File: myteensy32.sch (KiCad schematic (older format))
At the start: 1 part

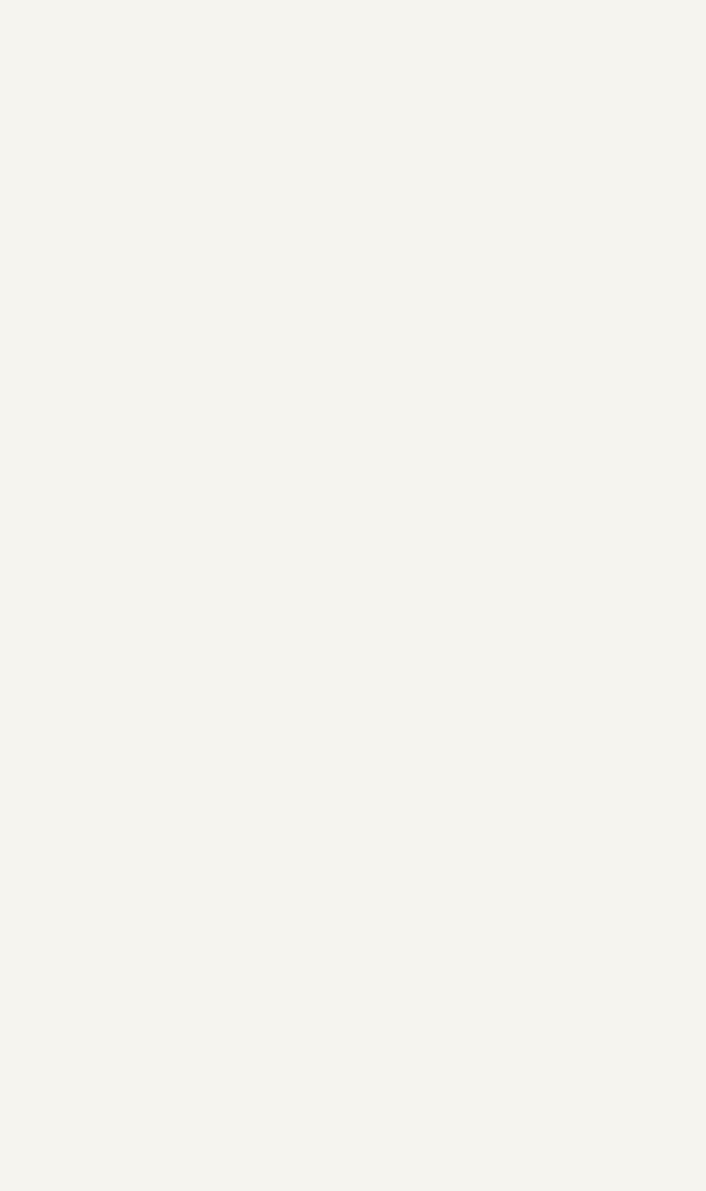
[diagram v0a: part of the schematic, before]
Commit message: add sym mk20dx256vlh7
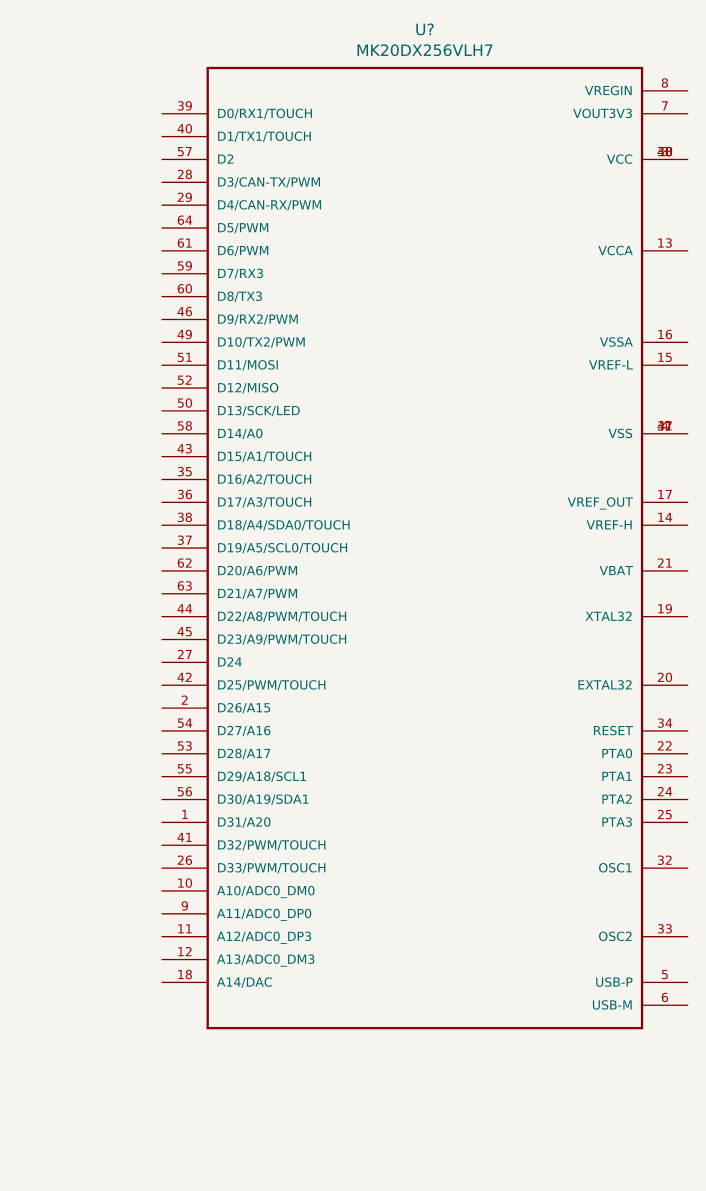
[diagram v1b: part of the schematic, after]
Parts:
- added U?: MK20DX256VLH7, QFP50P1200X1200X160-64N, symbol mylib:MK20DX256VLH7
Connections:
- new net: U?.3 (VCC), U?.30 (VCC), U?.48 (VCC)
- new net: U?.31 (VSS), U?.4 (VSS), U?.47 (VSS)
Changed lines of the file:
@@
+	1    0    0    -1
+$EndComp
+$Comp
+L mylib:MK20DX256VLH7 U?
+U 1 1 5F4A22C6
+P 8050 3500
+F 0 "U?" H 8100 5867 50  0000 C CNN
+F 1 "MK20DX256VLH7" H 8100 5776 50  0000 C CNN
+F 2 "QFP50P1200X1200X160-64N" H 8050 3500 50  0001 L BNN
+F 3 "" H 8050 3500 50  0001 C CNN
+	1    8050 3500
 	1    0    0    -1
 $EndComp

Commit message: シンボルのの作り方が雑だったので心配したけど大丈夫そうだった。
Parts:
- removed U?: MK20DX256VLH7, QFP50P1200X1200X160-64N, symbol mylib:MK20DX256VLH7
- added U2: MK20DX256VLH7, mylib:QFP50P1200X1200X160-64N, symbol mylib:MK20DX256VLH7
- gave numbers to parts that had none: 1
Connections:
- net at U1.25 (PTB5/IRQ_16): now also U2.31 (VSS), U2.4 (VSS), U2.47 (VSS)
- new net: U2.3 (VCC), U2.30 (VCC), U2.48 (VCC)
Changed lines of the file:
@@
 $EndDescr
 $Comp
-L MCU_NXP_Kinetis:MKL04Z32VLC4 U?
+L MCU_NXP_Kinetis:MKL04Z32VLC4 U1
 U 1 1 5F49FA87
 P 4450 4650
-F 0 "U?" H 4450 6631 50  0000 C CNN
+F 0 "U1" H 4450 6631 50  0000 C CNN
 F 1 "MKL04Z32VLC4" H 4450 6540 50  0000 C CNN
 F 2 "Package_QFP:LQFP-32_7x7mm_P0.8mm" H 4600 3025 50  0001 L TNN
@@
 $EndComp
 $Comp
-L mylib:MK20DX256VLH7 U?
-U 1 1 5F4A22C6
-P 8050 3500
-F 0 "U?" H 8100 5867 50  0000 C CNN
-F 1 "MK20DX256VLH7" H 8100 5776 50  0000 C CNN
-F 2 "QFP50P1200X1200X160-64N" H 8050 3500 50  0001 L BNN
-F 3 "" H 8050 3500 50  0001 C CNN
-	1    8050 3500
+L mylib:MK20DX256VLH7 U2
+U 1 1 5F4A610C
+P 8250 4000
+F 0 "U2" H 8300 6367 50  0000 C CNN
+F 1 "MK20DX256VLH7" H 8300 6276 50  0000 C CNN
+F 2 "mylib:QFP50P1200X1200X160-64N" H 8250 4000 50  0001 L BNN
+F 3 "" H 8250 4000 50  0001 C CNN
+	1    8250 4000
 	1    0    0    -1
 $EndComp
+Wire Wire Line
+	9450 3400 10300 3400
+Wire Wire Line
+	10300 3400 10300 1400
+Wire Wire Line
+	10300 1400 6400 1400
+Wire Wire Line
+	6400 4150 5850 4150
+Wire Wire Line
+	6400 1400 6400 4150
 $EndSCHEMATC

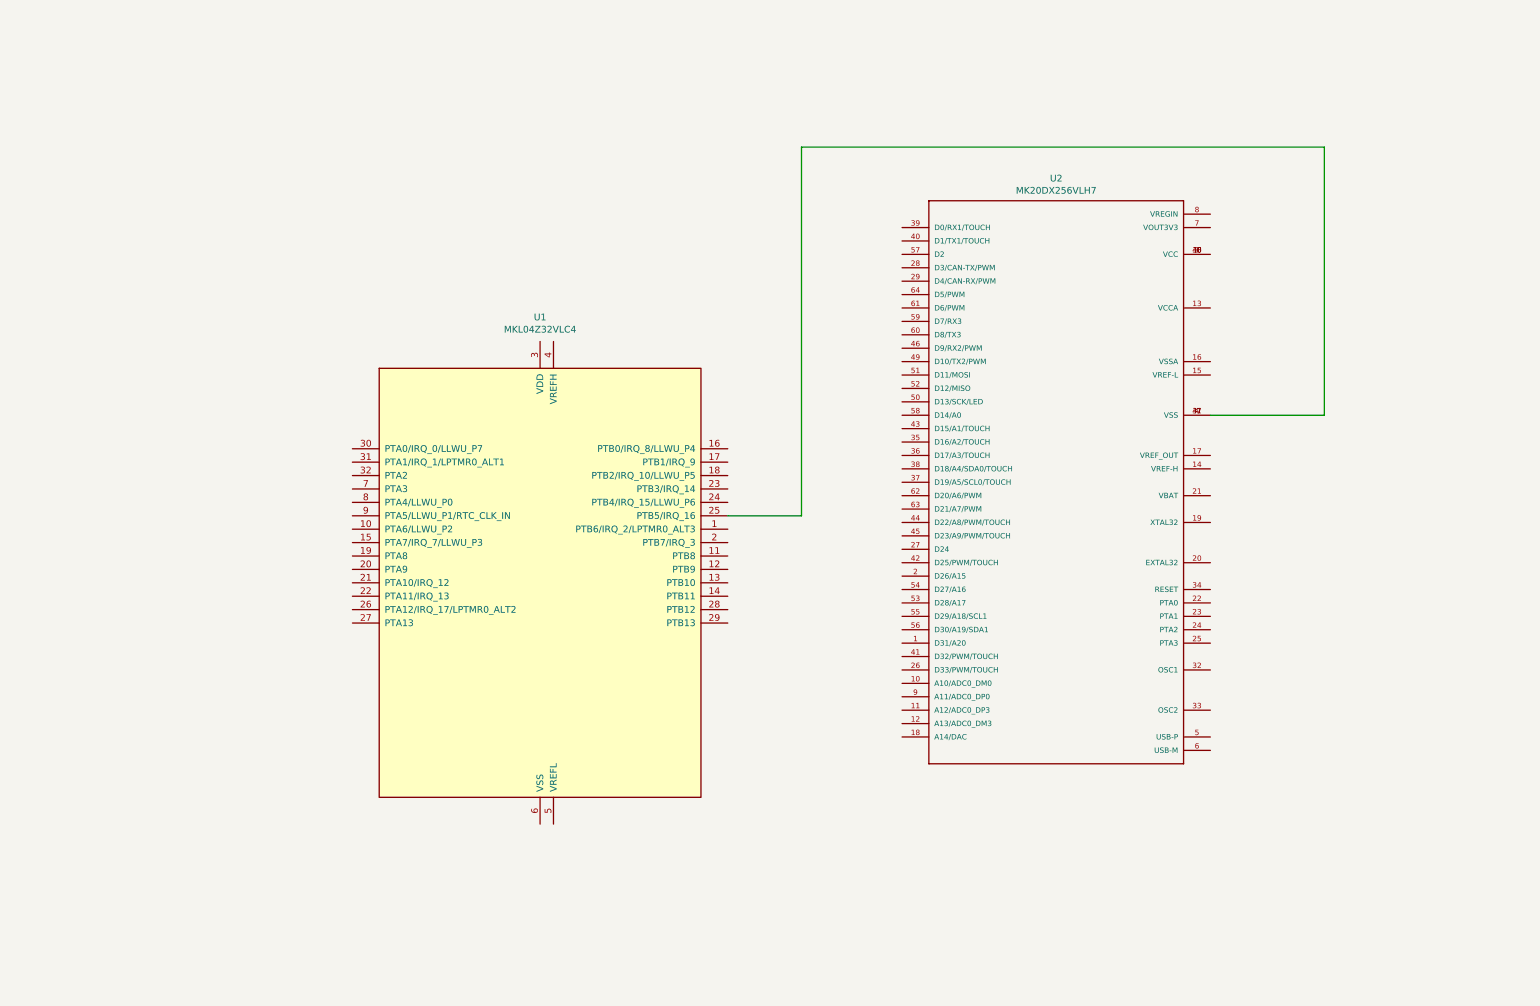
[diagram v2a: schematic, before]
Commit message: mkl04z32vlc4周辺の配線ができた
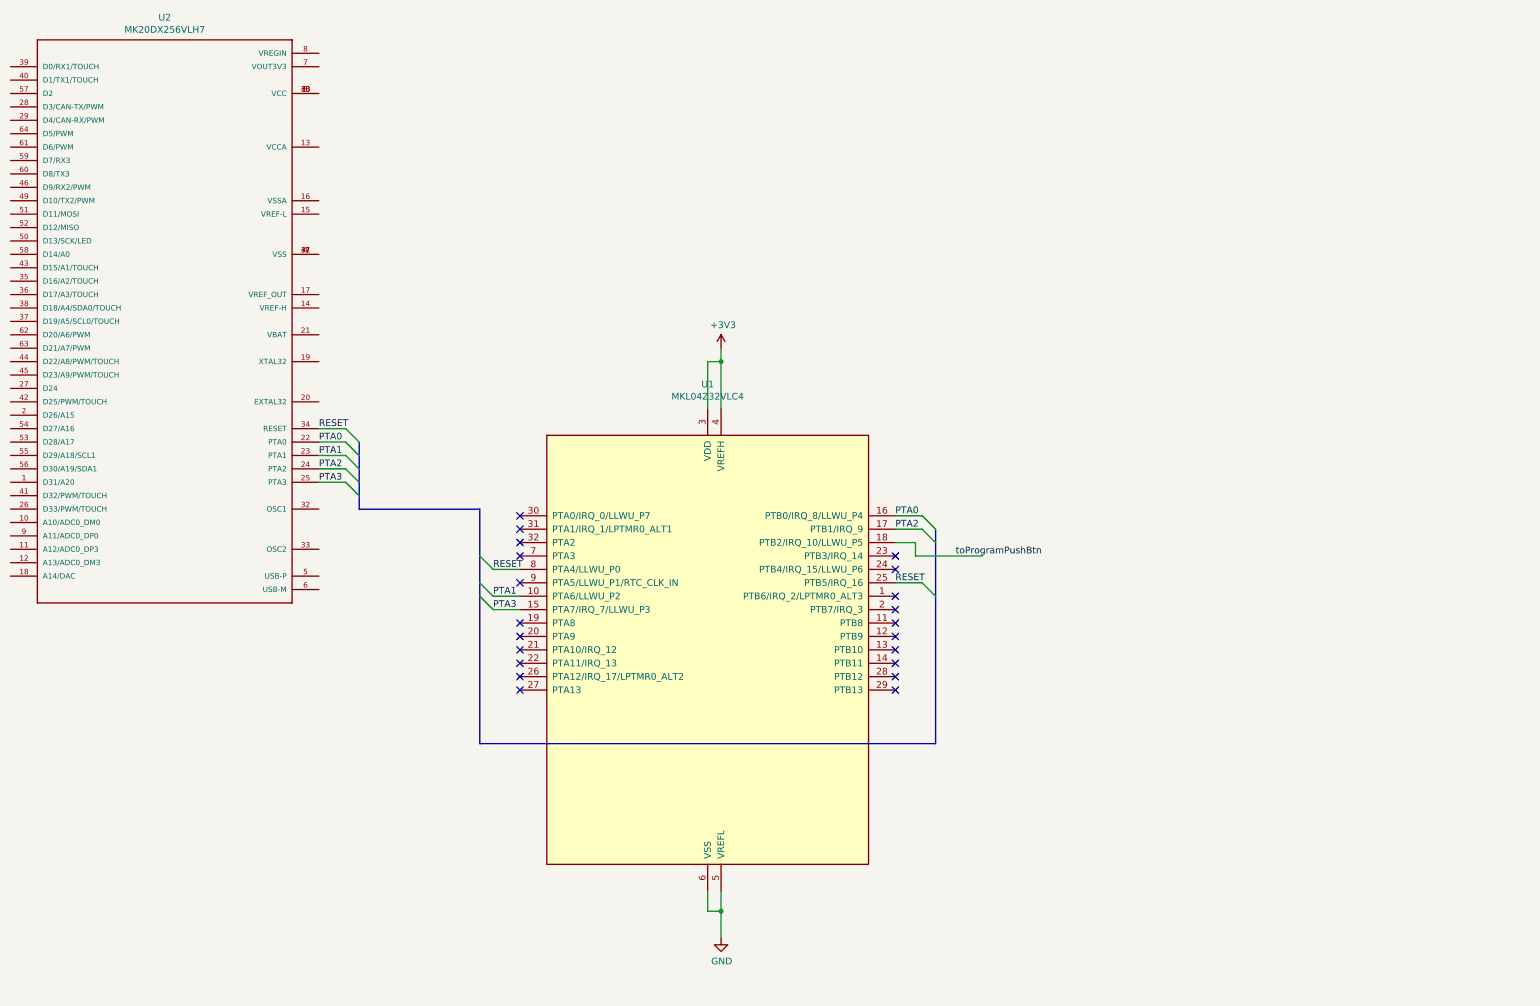
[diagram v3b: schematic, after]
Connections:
- net labels added: +3V3, GND, PTA0, PTA1, PTA2, PTA3, RESET, toProgramPushBtn
- wire segments 5 -> 22
- no-connect marks 0 -> 21
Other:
- moved on the sheet: U1, U2
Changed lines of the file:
@@
 $EndDescr
+$Comp
+L mylib:MK20DX256VLH7 U2
+U 1 1 5F4A610C
+P 1600 2800
+F 0 "U2" H 1650 5167 50  0000 C CNN
+F 1 "MK20DX256VLH7" H 1650 5076 50  0000 C CNN
+F 2 "mylib:QFP50P1200X1200X160-64N" H 1600 2800 50  0001 L BNN
+F 3 "" H 1600 2800 50  0001 C CNN
+	1    1600 2800
+	1    0    0    -1
+$EndComp
+Wire Wire Line
+	2800 3500 3000 3500
+Text Label 2800 3500 0    50   ~ 0
+RESET
+Wire Wire Line
+	2800 3600 3000 3600
+Wire Wire Line
+	2800 3700 3000 3700
+Wire Wire Line
+	2800 3800 3000 3800
+Wire Wire Line
+	2800 3900 3000 3900
+Text Label 2800 3600 0    50   ~ 0
+PTA0
+Text Label 2800 3700 0    50   ~ 0
+PTA1
+Text Label 2800 3800 0    50   ~ 0
+PTA2
+Text Label 2800 3900 0    50   ~ 0
+PTA3
+Entry Wire Line
+	3000 3500 3100 3600
+Entry Wire Line
+	3000 3600 3100 3700
+Entry Wire Line
+	3000 3700 3100 3800
+Entry Wire Line
+	3000 3800 3100 3900
+Entry Wire Line
+	3000 3900 3100 4000
+Wire Bus Line
+	3100 3600 3100 4100
+$Comp
+L power:GND #PWR?
+U 1 1 5F4B89CA
+P 5800 7300
+F 0 "#PWR?" H 5800 7050 50  0001 C CNN
+F 1 "GND" H 5805 7127 50  0000 C CNN
+F 2 "" H 5800 7300 50  0001 C CNN
+F 3 "" H 5800 7300 50  0001 C CNN
+	1    5800 7300
+	1    0    0    -1
+$EndComp
+Connection ~ 5800 7100
+Wire Bus Line
+	4000 4100 4000 5850
+Wire Bus Line
+	7400 4250 7400 5850
+Wire Wire Line
+	5800 7100 5800 7300
+Wire Wire Line
+	5800 7100 5800 6950
+Wire Wire Line
+	5700 7100 5800 7100
+Wire Wire Line
+	5700 6950 5700 7100
+Connection ~ 5800 3000
+Wire Wire Line
+	5800 2900 5800 3000
+$Comp
+L power:+3V3 #PWR?
+U 1 1 5F4B7C1C
+P 5800 2900
+F 0 "#PWR?" H 5800 2750 50  0001 C CNN
+F 1 "+3V3" H 5815 3073 50  0000 C CNN
+F 2 "" H 5800 2900 50  0001 C CNN
+F 3 "" H 5800 2900 50  0001 C CNN
+	1    5800 2900
+	1    0    0    -1
+$EndComp
+Wire Wire Line
+	5800 3000 5800 3350
+Wire Wire Line
+	5700 3000 5800 3000
+Wire Wire Line
+	5700 3350 5700 3000
+NoConn ~ 4300 4950
+NoConn ~ 4300 5050
+NoConn ~ 4300 5150
+NoConn ~ 4300 5250
+NoConn ~ 4300 5350
+NoConn ~ 4300 5450
+NoConn ~ 7100 5450
+NoConn ~ 7100 5350
+NoConn ~ 7100 5150
+NoConn ~ 7100 5250
+NoConn ~ 7100 5050
+NoConn ~ 7100 4950
+NoConn ~ 7100 4850
+NoConn ~ 7100 4750
+Text Label 7550 4450 0    50   ~ 0
+toProgramPushBtn
+Wire Wire Line
+	7250 4450 7750 4450
+Wire Wire Line
+	7250 4350 7250 4450
+Wire Wire Line
+	7100 4350 7250 4350
+Text Label 7100 4650 0    50   ~ 0
+RESET
+Text Label 4100 4550 0    50   ~ 0
+RESET
+Text Label 4100 4850 0    50   ~ 0
+PTA3
+Text Label 7100 4250 0    50   ~ 0
+PTA2
+Text Label 4100 4750 0    50   ~ 0
+PTA1
+Text Label 7100 4150 0    50   ~ 0
+PTA0
+Wire Bus Line
+	4000 5850 7400 5850
+Wire Bus Line
+	3100 4100 4000 4100
+Entry Wire Line
+	7300 4650 7400 4750
+Entry Wire Line
+	7300 4250 7400 4350
+Entry Wire Line
+	7300 4150 7400 4250
+Entry Wire Line
+	4000 4450 4100 4550
+Entry Wire Line
+	4000 4650 4100 4750
+Entry Wire Line
+	4000 4750 4100 4850
+Wire Wire Line
+	7100 4650 7300 4650
+NoConn ~ 7100 4550
+NoConn ~ 7100 4450
+NoConn ~ 4300 4650
+NoConn ~ 4300 4450
+NoConn ~ 4300 4350
+NoConn ~ 4300 4250
+NoConn ~ 4300 4150
+Wire Wire Line
+	4300 4550 4100 4550
+Wire Wire Line
+	4300 4750 4100 4750
+Wire Wire Line
+	7300 4250 7100 4250
+Wire Wire Line
+	7300 4150 7100 4150
+Wire Wire Line
+	4300 4850 4100 4850
 $Comp
 L MCU_NXP_Kinetis:MKL04Z32VLC4 U1
 U 1 1 5F49FA87
-P 4450 4650
-F 0 "U1" H 4450 6631 50  0000 C CNN
-F 1 "MKL04Z32VLC4" H 4450 6540 50  0000 C CNN
-F 2 "Package_QFP:LQFP-32_7x7mm_P0.8mm" H 4600 3025 50  0001 L TNN
-F 3 "http://www.nxp.com/docs/en/data-sheet/KL04P48M48SF1.pdf" H 4750 2850 50  0001 L BNN
-	1    4450 4650
+P 5700 5150
+F 0 "U1" H 5700 7131 50  0000 C CNN
+F 1 "MKL04Z32VLC4" H 5700 7040 50  0000 C CNN
+F 2 "Package_QFP:LQFP-32_7x7mm_P0.8mm" H 5850 3525 50  0001 L TNN
+F 3 "http://www.nxp.com/docs/en/data-sheet/KL04P48M48SF1.pdf" H 6000 3350 50  0001 L BNN
+	1    5700 5150
 	1    0    0    -1
 $EndComp
-$Comp
-L mylib:MK20DX256VLH7 U2
-U 1 1 5F4A610C
-P 8250 4000
-F 0 "U2" H 8300 6367 50  0000 C CNN
-F 1 "MK20DX256VLH7" H 8300 6276 50  0000 C CNN
-F 2 "mylib:QFP50P1200X1200X160-64N" H 8250 4000 50  0001 L BNN
-F 3 "" H 8250 4000 50  0001 C CNN
-	1    8250 4000
-	1    0    0    -1
-$EndComp
-Wire Wire Line
-	9450 3400 10300 3400
-Wire Wire Line
-	10300 3400 10300 1400
-Wire Wire Line
-	10300 1400 6400 1400
-Wire Wire Line
-	6400 4150 5850 4150
-Wire Wire Line
-	6400 1400 6400 4150
 $EndSCHEMATC

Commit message: usb,Crystal等周辺回路の追加
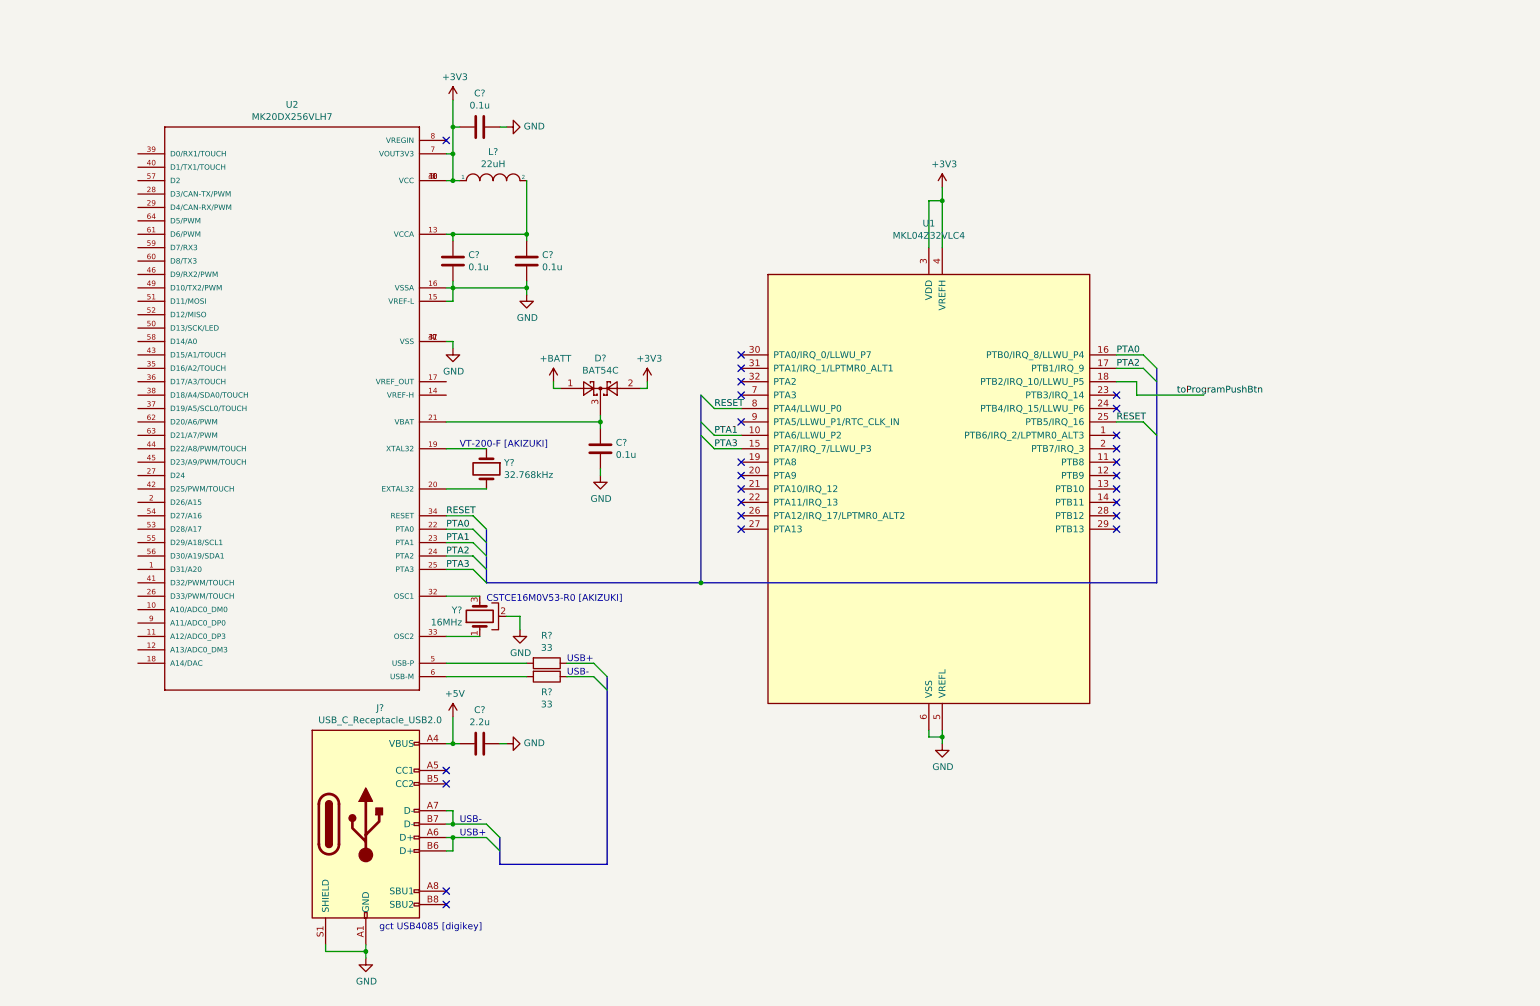
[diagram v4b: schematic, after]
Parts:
- added C? (x4): 0.1u, symbol Device:C
- added C?: 2.2u, symbol Device:C
- added D?: BAT54C, Package_TO_SOT_SMD:SOT-23, symbol Diode:BAT54C
- added J?: USB_C_Receptacle_USB2.0, symbol Connector:USB_C_Receptacle_USB2.0
- added L?: 22uH, symbol pspice:INDUCTOR
- added R? (x2): 33, symbol Device:R
- added Y?: 32.768kHz, symbol Device:Crystal
- added Y?: 16MHz, symbol Device:Crystal_GND2
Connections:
- net labels added: +5V, +BATT
- wire segments 22 -> 78
- no-connect marks 21 -> 26
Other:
- note added: "CSTCE16M0V53-R0 [AKIZUKI]"
- note added: "USB+"
- note added: "USB-"
- note added: "VT-200-F [AKIZUKI]"
- note added: "gct USB4085 [digikey]"
- moved on the sheet: U1, U2
